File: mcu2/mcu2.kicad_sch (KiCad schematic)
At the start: 19 parts, among them J1 24VIN, J2 Conn_01x26, Q1 WSF3085, Q2 PL4009, Q3 PL4009, U1 rp2040_zero, U2 motor_driver

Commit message: adjust holes and silkscreen
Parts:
- C2: footprint Capacitor_SMD:CP_Elec_6.3x5.4 -> Capacitor_SMD:CP_Elec_6.3x7.7
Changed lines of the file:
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@@
       (effects (font (size 1.27 1.27)) (justify left))
     )
-    (property "Footprint" "Capacitor_SMD:CP_Elec_6.3x5.4" (id 2) (at 182.5752 104.14 0)
+    (property "Footprint" "Capacitor_SMD:CP_Elec_6.3x7.7" (id 2) (at 182.5752 104.14 0)
       (effects (font (size 1.27 1.27)) hide)
     )
@@
     )
     (path "/e2efdb57-d4a9-42a3-8b7f-aa4cdff50a39"
-      (reference "C2") (unit 1) (value "100u/35V") (footprint "Capacitor_SMD:CP_Elec_6.3x5.4")
+      (reference "C2") (unit 1) (value "100u/35V") (footprint "Capacitor_SMD:CP_Elec_6.3x7.7")
     )
     (path "/09c48721-96f9-49c8-aa3e-cea6dd620691"

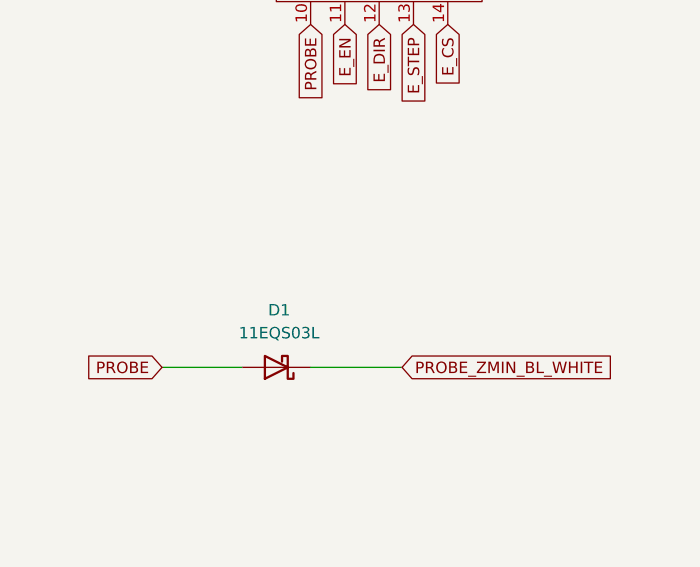
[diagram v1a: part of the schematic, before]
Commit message: smd schottky and jumper, ordered JLCPCB
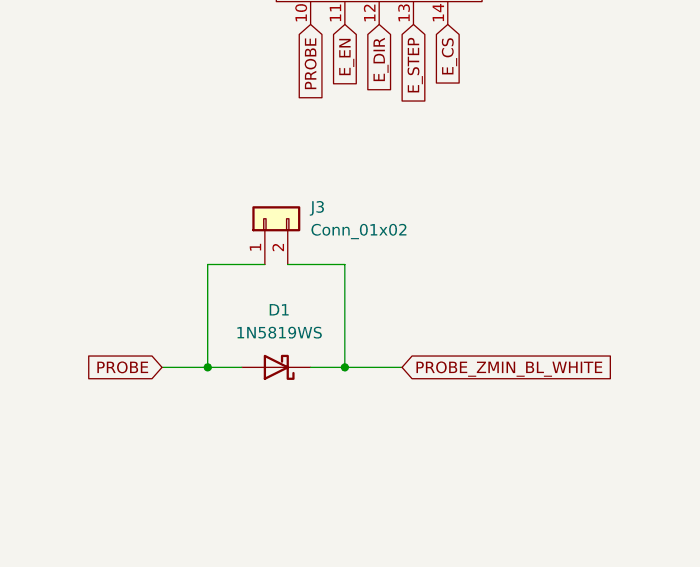
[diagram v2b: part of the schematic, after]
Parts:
- added J3: Conn_01x02, Connector_PinHeader_2.54mm:PinHeader_1x02_P2.54mm_Vertical, symbol Connector_Generic:Conn_01x02
- D1: value 11EQS03L -> 1N5819WS; footprint Diode_THT:D_A-405_P7.62mm_Horizontal -> Diode_SMD:D_SOD-323_HandSoldering
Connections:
- net PROBE: now also J3.1 (Pin_1)
- net PROBE_ZMIN_BL_WHITE: now also J3.2 (Pin_2)
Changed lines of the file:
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@@
 (kicad_sch (version 20211123) (generator eeschema)
   (paper "A4")
+  (junction (at 44.45 114.3) (diameter 0) (color 0 0 0 0)
+  )
   (junction (at 133.35 66.04) (diameter 0) (color 0 0 0 0)
   )
@@
   )
   (junction (at 133.35 172.72) (diameter 0) (color 0 0 0 0)
+  )
+  (junction (at 59.69 114.3) (diameter 0) (color 0 0 0 0)
   )
   (junction (at 133.35 153.67) (diameter 0) (color 0 0 0 0)
@@
     (stroke (width 0) (type default) (color 0 0 0 0))
   )
+  (wire (pts (xy 53.34 102.87) (xy 59.69 102.87))
+    (stroke (width 0) (type default) (color 0 0 0 0))
+  )
   (wire (pts (xy 52.07 167.64) (xy 52.07 172.72))
     (stroke (width 0) (type default) (color 0 0 0 0))
@@
     (stroke (width 0) (type default) (color 0 0 0 0))
   )
+  (wire (pts (xy 50.8 102.87) (xy 44.45 102.87))
+    (stroke (width 0) (type default) (color 0 0 0 0))
+  )
+  (wire (pts (xy 59.69 114.3) (xy 66.04 114.3))
+    (stroke (width 0) (type default) (color 0 0 0 0))
+  )
+  (wire (pts (xy 44.45 102.87) (xy 44.45 114.3))
+    (stroke (width 0) (type default) (color 0 0 0 0))
+  )
   (wire (pts (xy 43.18 162.56) (xy 43.18 166.37))
     (stroke (width 0) (type default) (color 0 0 0 0))
@@
     (stroke (width 0) (type default) (color 0 0 0 0))
   )
-  (wire (pts (xy 55.88 114.3) (xy 66.04 114.3))
+  (wire (pts (xy 55.88 114.3) (xy 59.69 114.3))
+    (stroke (width 0) (type default) (color 0 0 0 0))
+  )
+  (wire (pts (xy 44.45 114.3) (xy 48.26 114.3))
     (stroke (width 0) (type default) (color 0 0 0 0))
   )
@@
     (stroke (width 0) (type default) (color 0 0 0 0))
   )
+  (wire (pts (xy 59.69 102.87) (xy 59.69 114.3))
+    (stroke (width 0) (type default) (color 0 0 0 0))
+  )
   (wire (pts (xy 133.35 105.41) (xy 133.35 102.87))
     (stroke (width 0) (type default) (color 0 0 0 0))
@@
     (stroke (width 0) (type default) (color 0 0 0 0))
   )
-  (wire (pts (xy 39.37 114.3) (xy 48.26 114.3))
+  (wire (pts (xy 39.37 114.3) (xy 44.45 114.3))
     (stroke (width 0) (type default) (color 0 0 0 0))
   )
@@
     (in_bom yes) (on_board yes) (fields_autoplaced)
     (property "Reference" "D1" (id 0) (at 52.3875 107.95 0))
-    (property "Value" "11EQS03L" (id 1) (at 52.3875 110.49 0))
-    (property "Footprint" "Diode_THT:D_A-405_P7.62mm_Horizontal" (id 2) (at 52.07 114.3 0)
+    (property "Value" "1N5819WS" (id 1) (at 52.3875 110.49 0))
+    (property "Footprint" "Diode_SMD:D_SOD-323_HandSoldering" (id 2) (at 52.07 114.3 0)
       (effects (font (size 1.27 1.27)) hide)
     )
@@
     )
     (pin "1")
+  )
+  (symbol (lib_id "Connector_Generic:Conn_01x02") (at 50.8 97.79 90) (unit 1)
+    (in_bom yes) (on_board yes) (fields_autoplaced)
+    (property "Reference" "J3" (id 0) (at 55.88 96.5199 90)
+      (effects (font (size 1.27 1.27)) (justify right))
+    )
+    (property "Value" "Conn_01x02" (id 1) (at 55.88 99.0599 90)
+      (effects (font (size 1.27 1.27)) (justify right))
+    )
+    (property "Footprint" "Connector_PinHeader_2.54mm:PinHeader_1x02_P2.54mm_Vertical" (id 2) (at 50.8 97.79 0)
+      (effects (font (size 1.27 1.27)) hide)
+    )
+    (property "Datasheet" "~" (id 3) (at 50.8 97.79 0)
+      (effects (font (size 1.27 1.27)) hide)
+    )
+    (pin "1")
+    (pin "2")
   )
   (symbol (lib_id "power:GND") (at 133.35 74.93 0) (unit 1)
@@
     )
     (path "/09c48721-96f9-49c8-aa3e-cea6dd620691"
-      (reference "D1") (unit 1) (value "11EQS03L") (footprint "Diode_THT:D_A-405_P7.62mm_Horizontal")
+      (reference "D1") (unit 1) (value "1N5819WS") (footprint "Diode_SMD:D_SOD-323_HandSoldering")
     )
     (path "/f545ca7c-28a3-4fa9-87c0-4fde6e2543c8"
@@
       (reference "J2") (unit 1) (value "Conn_01x26") (footprint "FFCconnector:FFC26pinTH")
     )
+    (path "/63e17293-d2f1-4991-8dd7-503cf3d5ab8f"
+      (reference "J3") (unit 1) (value "Conn_01x02") (footprint "Connector_PinHeader_2.54mm:PinHeader_1x02_P2.54mm_Vertical")
+    )
     (path "/2822508c-4c59-4b8f-9916-8155a4404ab8"

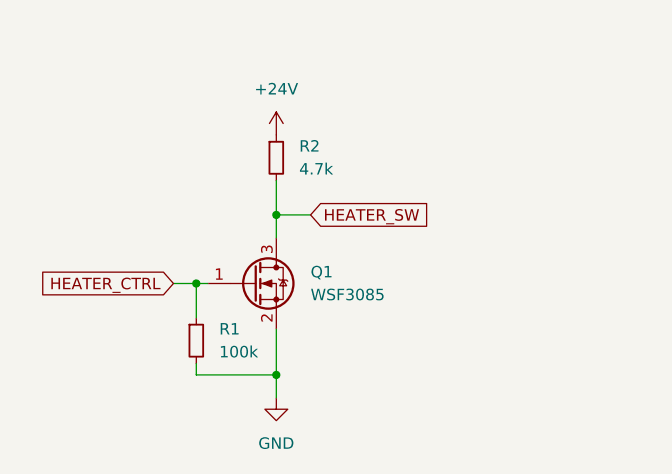
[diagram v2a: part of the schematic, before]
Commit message: change footprint on heater mos
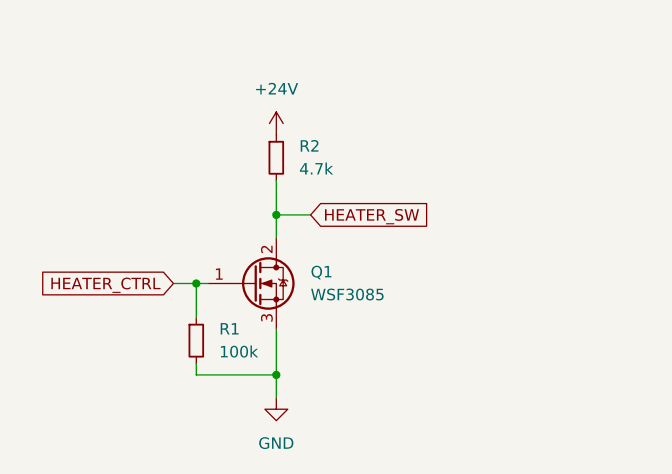
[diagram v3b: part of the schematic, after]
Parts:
- removed Q1: WSF3085, Package_TO_SOT_SMD:TO-252-3_TabPin2, symbol Device:Q_NMOS_GSD
- added Q1: WSF3085, Package_TO_SOT_SMD:TO-252-2, symbol Device:Q_NMOS_GDS
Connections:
- net GND: now also Q1.3 (S)
- net HEATER_CTRL: now also Q1.1 (G)
- net HEATER_SW: now also Q1.2 (D)
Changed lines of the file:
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@@
     (pin "2")
-  )
-  (symbol (lib_id "Device:Q_NMOS_GSD") (at 49.53 162.56 0) (unit 1)
-    (in_bom yes) (on_board yes) (fields_autoplaced)
-    (property "Reference" "Q1" (id 0) (at 55.88 161.2899 0)
-      (effects (font (size 1.27 1.27)) (justify left))
-    )
-    (property "Value" "WSF3085" (id 1) (at 55.88 163.8299 0)
-      (effects (font (size 1.27 1.27)) (justify left))
-    )
-    (property "Footprint" "Package_TO_SOT_SMD:TO-252-3_TabPin2" (id 2) (at 54.61 160.02 0)
-      (effects (font (size 1.27 1.27)) hide)
-    )
-    (property "Datasheet" "~" (id 3) (at 49.53 162.56 0)
-      (effects (font (size 1.27 1.27)) hide)
-    )
-    (pin "1")
-    (pin "2")
-    (pin "3")
   )
   (symbol (lib_id "Device:R_Small") (at 43.18 168.91 0) (unit 1)
@@
     (pin "1")
   )
+  (symbol (lib_id "Device:Q_NMOS_GDS") (at 49.53 162.56 0) (unit 1)
+    (in_bom yes) (on_board yes) (fields_autoplaced)
+    (property "Reference" "Q1" (id 0) (at 55.88 161.2899 0)
+      (effects (font (size 1.27 1.27)) (justify left))
+    )
+    (property "Value" "WSF3085" (id 1) (at 55.88 163.8299 0)
+      (effects (font (size 1.27 1.27)) (justify left))
+    )
+    (property "Footprint" "Package_TO_SOT_SMD:TO-252-2" (id 2) (at 54.61 160.02 0)
+      (effects (font (size 1.27 1.27)) hide)
+    )
+    (property "Datasheet" "~" (id 3) (at 49.53 162.56 0)
+      (effects (font (size 1.27 1.27)) hide)
+    )
+    (pin "1")
+    (pin "2")
+    (pin "3")
+  )
   (symbol (lib_id "Device:D_Zener") (at 198.12 100.33 270) (unit 1)
     (in_bom yes) (on_board yes) (fields_autoplaced)
@@
       (reference "J3") (unit 1) (value "Conn_01x02") (footprint "Connector_PinHeader_2.54mm:PinHeader_1x02_P2.54mm_Vertical")
     )
-    (path "/2822508c-4c59-4b8f-9916-8155a4404ab8"
-      (reference "Q1") (unit 1) (value "WSF3085") (footprint "Package_TO_SOT_SMD:TO-252-3_TabPin2")
+    (path "/ebda1544-61d5-4166-a2e9-fde8904cbfc1"
+      (reference "Q1") (unit 1) (value "WSF3085") (footprint "Package_TO_SOT_SMD:TO-252-2")
     )
     (path "/acafa3cf-c244-4d9a-b4e1-26e9844c9f41"

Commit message: r2 jlcpcb
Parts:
- added D3, D4, D5, D6: LED_0805, LED_SMD:LED_0805_2012Metric_Pad1.15x1.40mm_HandSolder, symbol Device:LED_Small
- added J4, J5, J6: Conn_01x01, Connector_PinHeader_2.54mm:PinHeader_1x01_P2.54mm_Vertical, symbol Connector_Generic:Conn_01x01
- added J7: Conn_01x02, Connector_PinHeader_2.54mm:PinHeader_1x02_P2.54mm_Vertical, symbol Connector_Generic:Conn_01x02
- added R9: 10k, Resistor_SMD:R_0805_2012Metric_Pad1.20x1.40mm_HandSolder, symbol Device:R_Small
- J1: value 24VIN -> KF128-5.08; footprint FFCconnector:SIP-2 -> FFCconnector:KF128-5.08
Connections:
- net +24V: now also R9.1
- net GND: now also D4.1 (K)
- net HEATER_SW: now also D3.1 (K), J4.1 (Pin_1); no longer R2.2
- net HOTEND_FAN_SW: now also D5.1 (K), J5.1 (Pin_1); no longer R6.2
- net PART_FAN_SW: now also D6.1 (K), J6.1 (Pin_1); no longer R7.2
- new net: D5.2 (A), R6.2
- new net: D3.2 (A), R2.2
- new net: D4.2 (A), R9.2
- new net: D6.2 (A), R7.2
- new net DIAG: J7.1 (Pin_1)
- new net INDEX: J7.2 (Pin_2)
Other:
- moved on the sheet: J1, Q1, Q3, R1, R2, R4, R6, R7

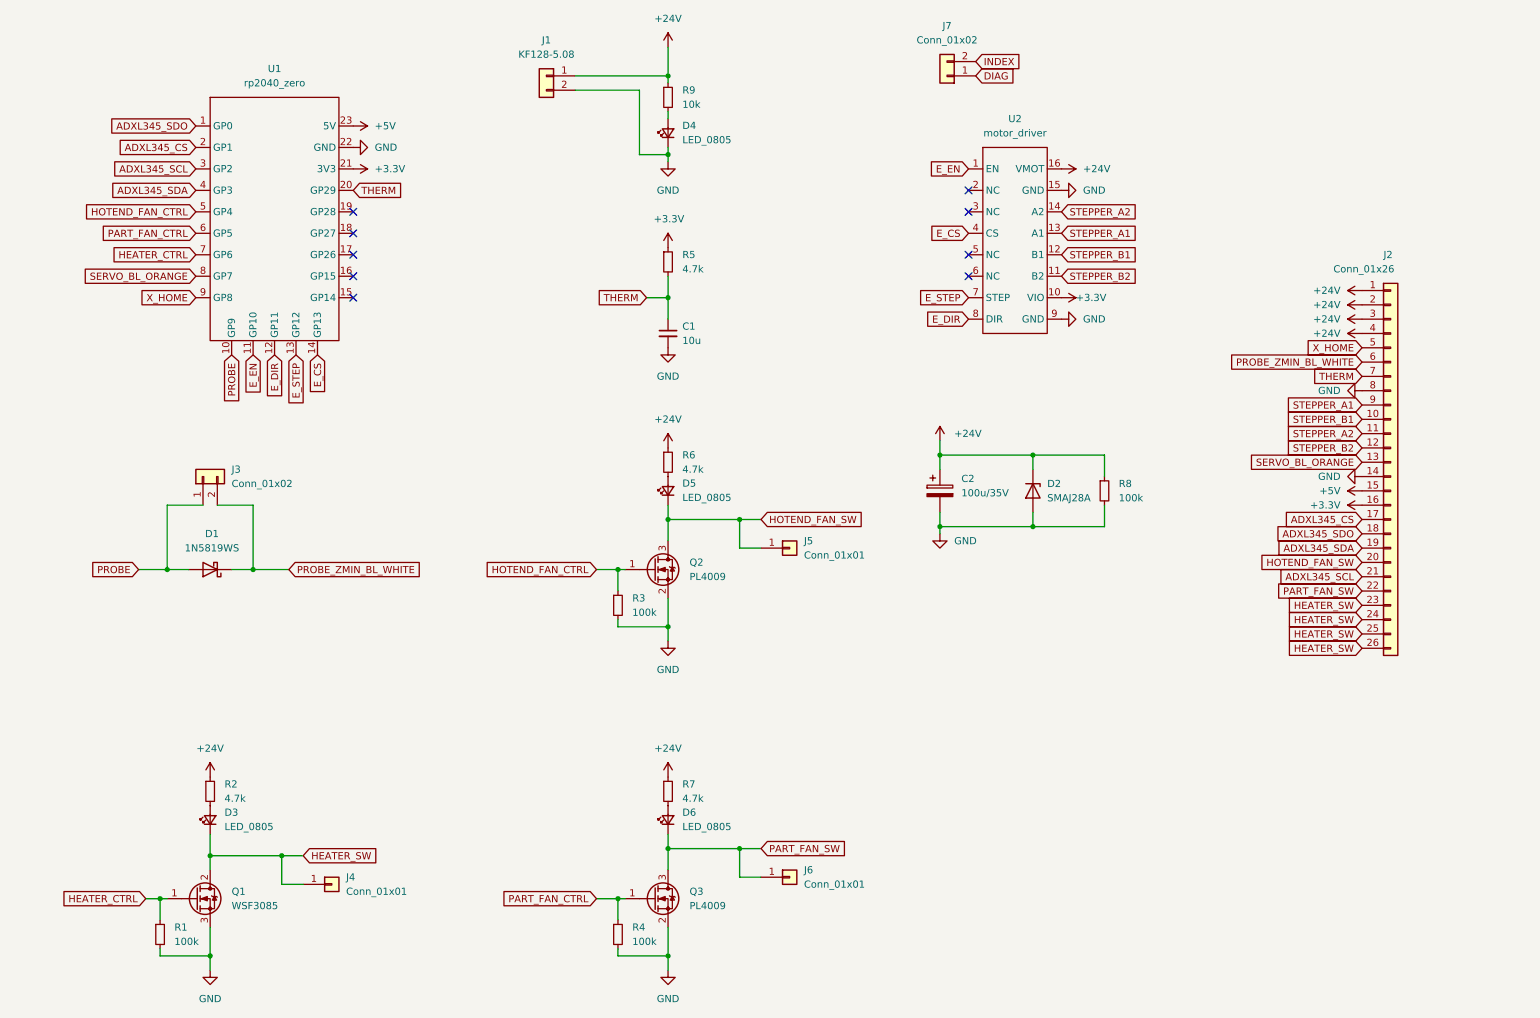
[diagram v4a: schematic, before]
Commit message: add a FFC connector on back side
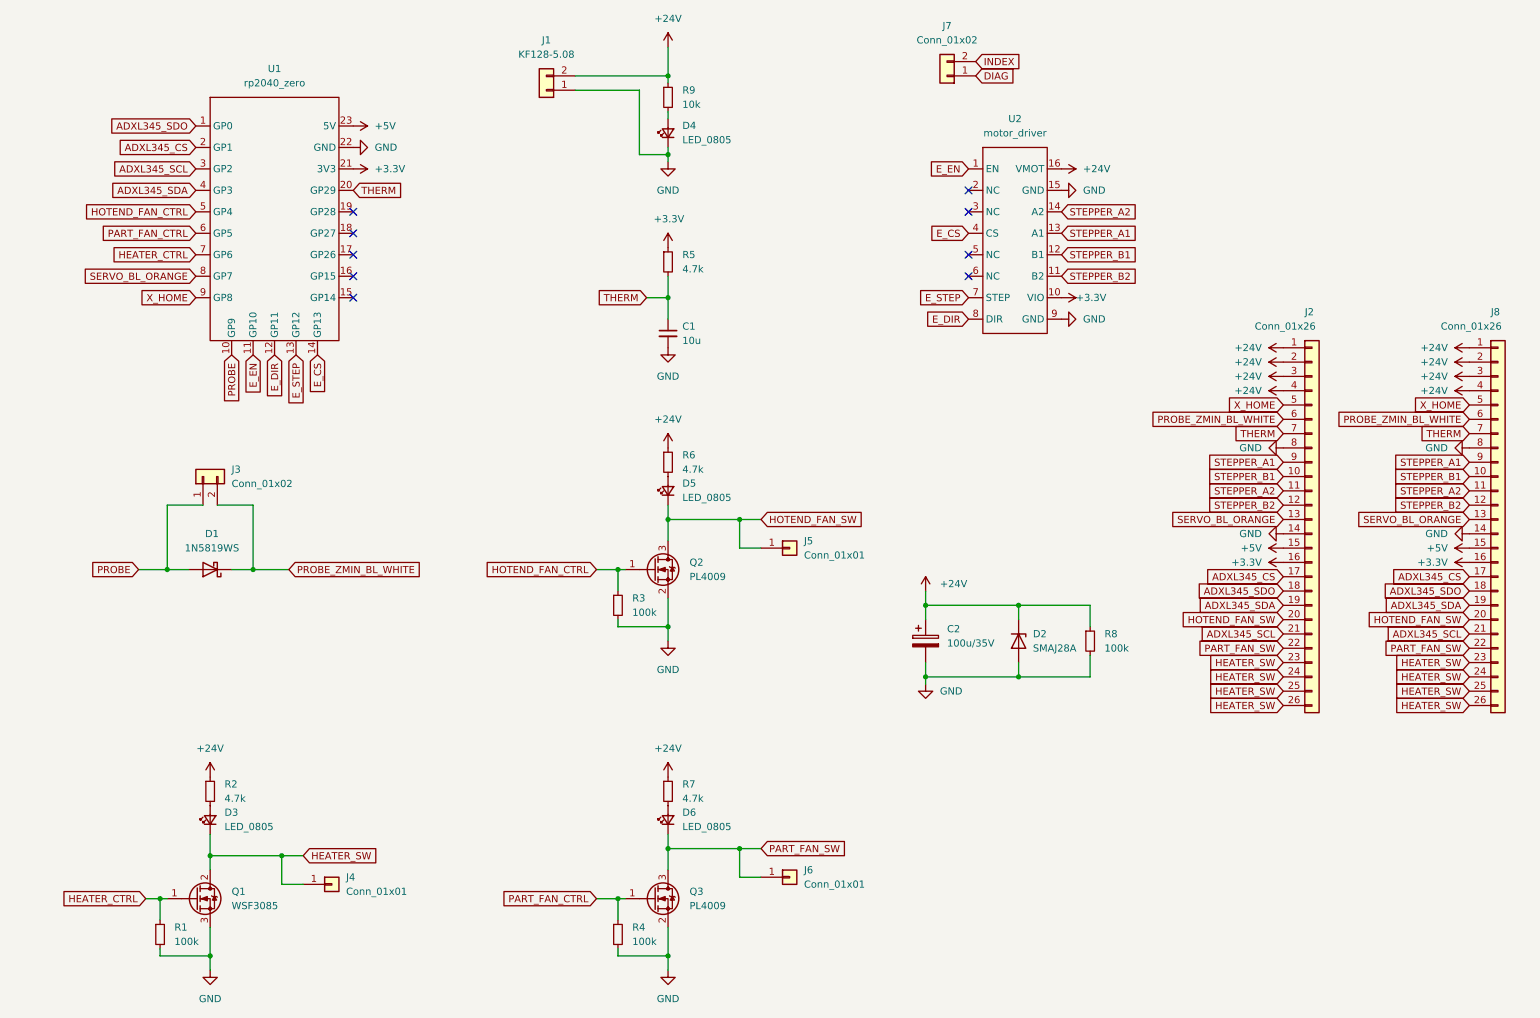
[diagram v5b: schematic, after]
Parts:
- added J8: Conn_01x26, FFCconnector:FFC26pinTH, symbol Connector_Generic:Conn_01x26
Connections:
- net +24V: now also J1.2 (Pin_2), J8.1 (Pin_1), J8.2 (Pin_2), J8.3 (Pin_3), J8.4 (Pin_4); no longer J1.1 (Pin_1)
- net +3V3: now also J8.16 (Pin_16)
- net +5V: now also J8.15 (Pin_15)
- net ADXL345_CS: now also J8.17 (Pin_17)
- net ADXL345_SCL: now also J8.21 (Pin_21)
- net ADXL345_SDA: now also J8.19 (Pin_19)
- net ADXL345_SDO: now also J8.18 (Pin_18)
- net GND: now also J1.1 (Pin_1), J8.14 (Pin_14), J8.8 (Pin_8); no longer J1.2 (Pin_2)
- net HEATER_SW: now also J8.23 (Pin_23), J8.24 (Pin_24), J8.25 (Pin_25), J8.26 (Pin_26)
- net HOTEND_FAN_SW: now also J8.20 (Pin_20)
- net PART_FAN_SW: now also J8.22 (Pin_22)
- net PROBE_ZMIN_BL_WHITE: now also J8.6 (Pin_6)
- net SERVO_BL_ORANGE: now also J8.13 (Pin_13)
- net STEPPER_A1: now also J8.9 (Pin_9)
- net STEPPER_A2: now also J8.11 (Pin_11)
- net STEPPER_B1: now also J8.10 (Pin_10)
- net STEPPER_B2: now also J8.12 (Pin_12)
- net THERM: now also J8.7 (Pin_7)
- net X_HOME: now also J8.5 (Pin_5)
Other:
- moved on the sheet: C2, D2, J1, J2, R8
